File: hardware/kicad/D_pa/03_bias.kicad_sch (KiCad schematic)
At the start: 30 parts, among them U20 MCP4922-E/SL, U21 MCP4922-E/SL, U31 INA240A1DR, U32 INA240A1DR, U33 INA240A1DR, U34 INA240A1DR, U41 LM358, U42 LM358

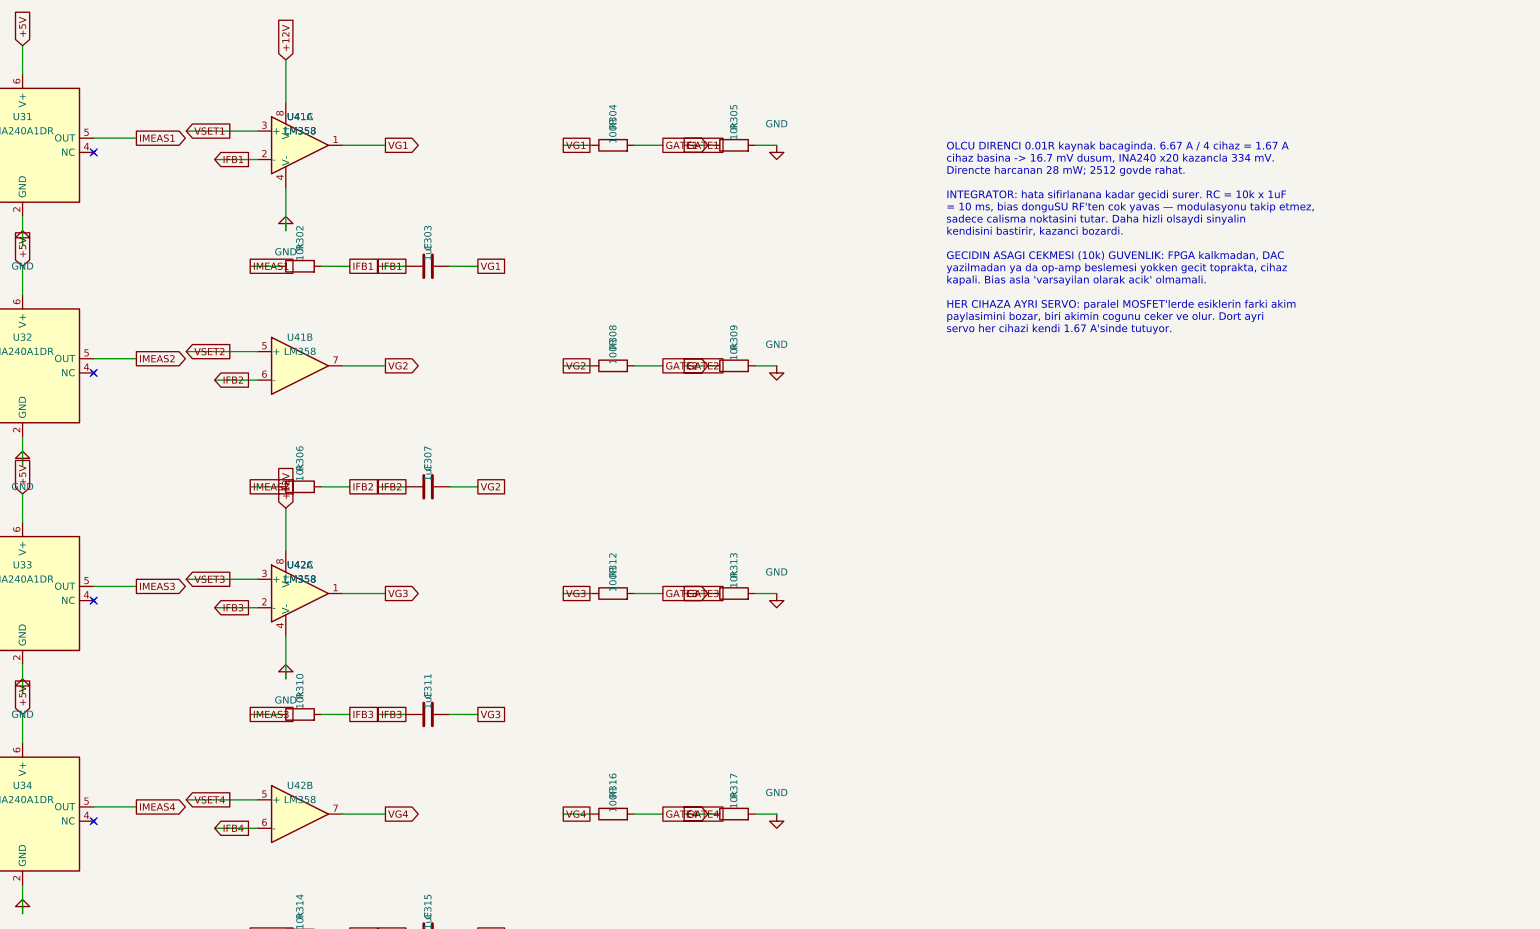
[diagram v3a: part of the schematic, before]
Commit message: Correct the clearance test for the pre-routed traces
The clearance test used a circle for each pad. The radius was
max(width, height)/2. The corner of a rectangle is at
hypot(width, height)/2 from the center. The test thus made the pad
smaller than it is. On the 2.5 x 4.5 mm gate pad of a TO-247 the
difference is 2.250 mm against 2.574 mm.

The DRN_A trace was on the gate pad of Q10 with an overlap of 35 um.
This is a short circuit between the 50 V drain rail and the gate of a
100 W device. The search that finds the tee offset accepted this
route. The overlap is at a corner and 35 um wide. You cannot see it
on a plot.

The test now uses the real shape of the pad and the collision test of
pcbnew. It also uses the 300 um clearance and not only an overlap. A
trace that is 50 um from a pad is also not possible to manufacture.

Board D was built again. No trace is below 300 um and the smallest
gap is 0.537 mm. Boards A and C were correct.
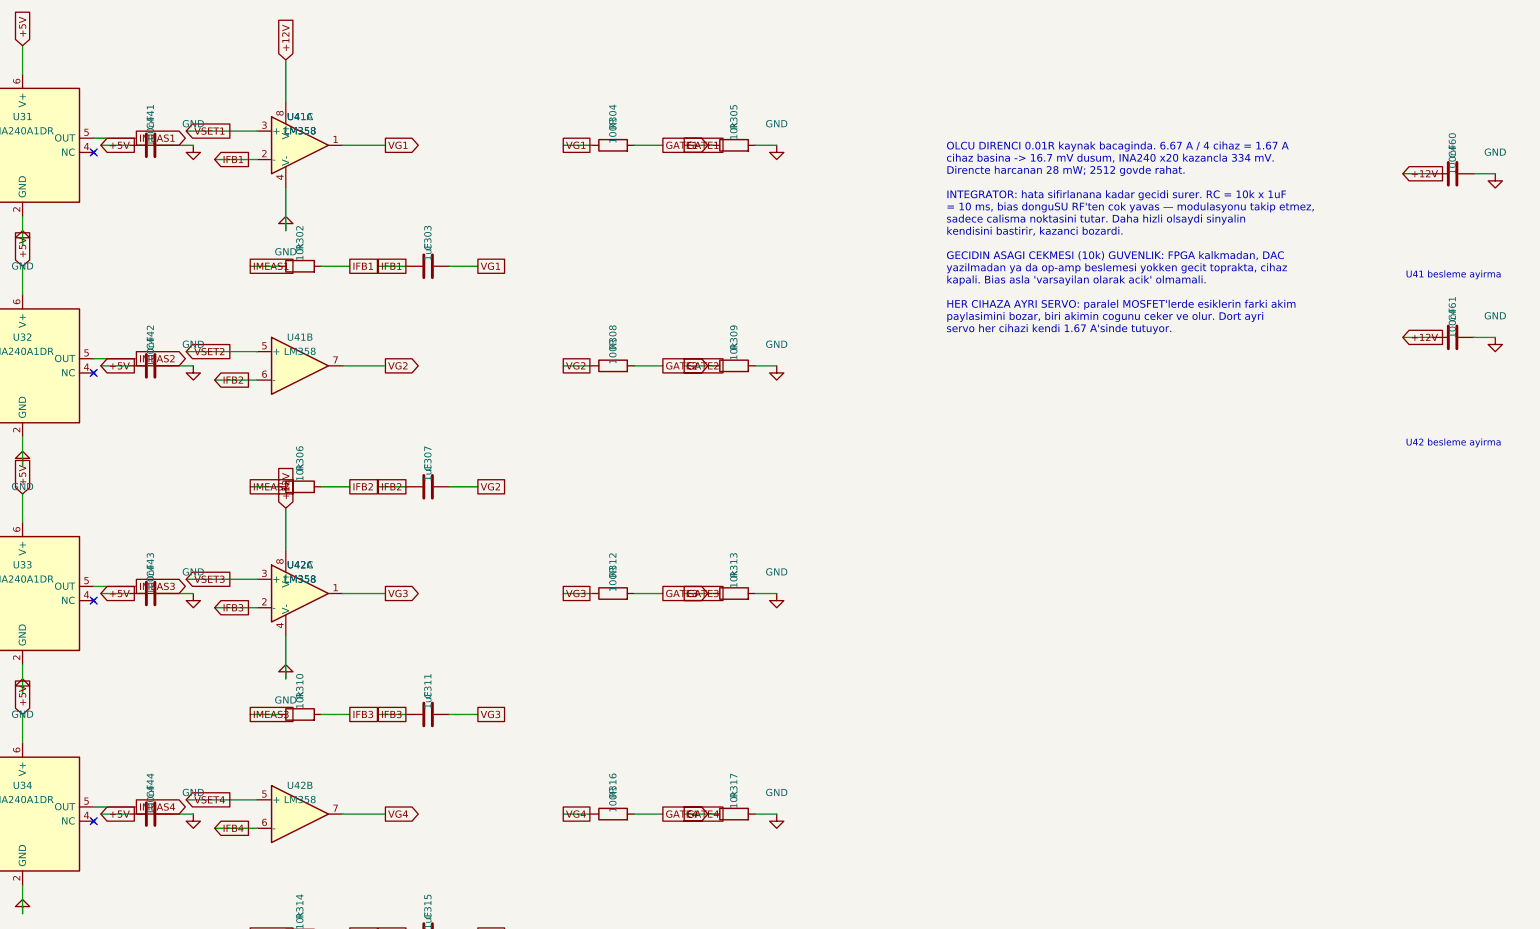
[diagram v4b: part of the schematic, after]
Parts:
- added C441, C442, C443, C444, C460, C461: 100nF, Capacitor_SMD:C_0603_1608Metric, symbol Device:C
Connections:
- net +12V: now also C460.1, C461.1
- net +5V: now also C441.1, C442.1, C443.1, C444.1
- net GND: now also C441.2, C442.2, C443.2, C444.2, C460.2, C461.2
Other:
- note added: "U41 besleme ayirma"
- note added: "U42 besleme ayirma"
